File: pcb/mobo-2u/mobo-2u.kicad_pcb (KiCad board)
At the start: 2 copper layers, 71.6 x 83 mm, 69 parts, among them J1 SWD_10, J2 PEEL_MOTOR, J3 DRIVE_MOTOR, J4 SW1, J5 SPRING_FINGERS, J6 SW2, J7 SW1, J8 USART1, J9 SWD_10, U1 STM32F031C6Tx, U2 STM32F031K6Ux, U4 AP1117-33, U5 MC34063AD, U6 MAX3078E, U7 DRV8837, U8 DRV8837, Y1 8MHz

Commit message: mega push, lots of cad updates, new pcb form factor and schematic rework
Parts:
- removed C12: 100uF, Capacitor_SMD:C_Elec_6.3x7.7
- removed C13, C9: 10u, Capacitor_SMD:C_0805_2012Metric
- removed C14: 470pF, Capacitor_SMD:C_0805_2012Metric
- removed D1: LED_RGBA, index:MHS110FRGBCT
- removed D6: 1N5819, Diode_SMD:D_SOD-123
- removed the G*** at (109.3, 62.5)
- removed the G*** at (80.0, 72.5)
- removed J4, J7: SW1, feeder:1TS003B-1400-3500A-CT
- removed J6: SW2, feeder:1TS003B-1400-3500A-CT
- removed L1: 220uH, Inductor_SMD:L_6.3x6.3_H3
- removed R2, R3, R5: 470, Resistor_SMD:R_0805_2012Metric
- removed REF**: OSHW-Symbol_6.7x6mm_Mask, feeder:OSHW-Symbol_6.7x6mm_Mask
- removed U1: STM32F031C6Tx, Package_QFP:LQFP-48_7x7mm_P0.5mm
- removed U4: AP1117-33, Package_TO_SOT_SMD:SOT-223-3_TabPin2
- added C15: 10u, Capacitor_SMD:C_0805_2012Metric, F.Cu at (89.3, 129.3)
- added C21: 10u, Capacitor_SMD:C_0805_2012Metric, F.Cu at (86.8, 129.3)
- added C22: 4.7n, Capacitor_SMD:C_0805_2012Metric, F.Cu at (81.3, 118.8)
- added C23: 47p, Capacitor_SMD:C_0805_2012Metric, F.Cu at (80.0, 115.8)
- added C24: 100n, Capacitor_SMD:C_0805_2012Metric, F.Cu at (83.5, 130.1)
- added C25: 10u, Capacitor_SMD:C_0805_2012Metric, F.Cu at (69.8, 117.3)
- added C26: 10u, Capacitor_SMD:C_0805_2012Metric, F.Cu at (69.8, 119.5)
- added C27: 10u, Capacitor_SMD:C_0805_2012Metric, F.Cu at (69.8, 115.0)
- added C28: 10u, Capacitor_SMD:C_0805_2012Metric, F.Cu at (75.6, 111.0)
- added C29: 0.1n, Capacitor_SMD:C_0805_2012Metric, F.Cu at (80.0, 113.3)
- added D4: B560C, Diode_SMD:D_SMC, F.Cu at (67.4, 126.5)
- added L2: 8.2uH, Inductor_SMD:L_Taiyo-Yuden_NR-50xx, F.Cu at (74.0, 124.7)
- added R10: 4.7k, Resistor_SMD:R_0805_2012Metric, F.Cu at (86.8, 124.0)
- added R11: 243k, Resistor_SMD:R_0805_2012Metric, F.Cu at (83.5, 122.0)
- added R12: 16.9k, Resistor_SMD:R_0805_2012Metric, F.Cu at (78.8, 118.8)
- added R18: 10k, Resistor_SMD:R_0805_2012Metric, F.Cu at (75.6, 120.5)
- added R19: 820R, Resistor_SMD:R_0805_2012Metric, F.Cu at (79.5, 122.0)
- added R8: 10k, Resistor_SMD:R_0805_2012Metric, F.Cu at (89.3, 124.0)
- added SW3: BACK_BTN, feeder:SKTDLDE010, F.Cu at (50.9, 99.3)
- added SW4: FWD_BTN, feeder:SKTDLDE010, F.Cu at (50.9, 83.0)
- added SW5: RESET_BTN, feeder:SKTDLDE010, F.Cu at (116.0, 55.8)
- added U3: STM32F030C8Tx, Package_QFP:LQFP-48_7x7mm_P0.5mm, F.Cu at (96.2, 107.9)
- added U9: TPS54560BDDA, Package_SO:Texas_R-PDSO-G8_EP2.95x4.9mm_Mask2.4x3.1mm_ThermalVias, F.Cu at (81.5, 126.0)
- added VDC: TP_24V, TestPoint:TestPoint_Pad_D2.0mm, F.Cu at (89.3, 120.4)
- C16: value 470uF -> 1u; footprint Capacitor_SMD:C_Elec_6.3x7.7 -> Capacitor_SMD:C_0805_2012Metric
- J9: footprint feeder:SWD-No-Paste -> Connector_PinHeader_1.27mm:PinHeader_2x05_P1.27mm_Vertical_SMD
- R13: value 0.33R -> 470
- R6: value 5.6k -> 470
- R9: value 39k -> 470
- U2: value STM32F031K6Ux -> MHS110FRGBCT; footprint feeder:QFN-32-No-Paste -> index:MHS110FRGBCT
- U5: value MC34063AD -> AP2210; footprint Package_SO:SOIC-8_3.9x4.9mm_P1.27mm -> Package_TO_SOT_SMD:SOT-23-5
- moved U2 53.9 mm to (95.4, 54.6), turned to 180 degrees
- moved PM1 27.9 mm to (61.8, 67.5)
- moved J2 26.4 mm to (60.0, 73.8), turned to -45 degrees
- moved PM2 23.9 mm to (65.0, 71.0)
- moved R6 23.3 mm to (82.8, 106.7), turned to 180 degrees
- moved R9 23.2 mm to (82.8, 104.5), turned to 180 degrees
- moved R13 18.9 mm to (82.8, 102.3), turned to 180 degrees
- moved R17 13.2 mm to (109.6, 57.1)
- moved U5 11.4 mm to (75.5, 114.5), turned to 90 degrees
- moved C16 9.61 mm to (75.5, 118.0)
- moved R7 7.86 mm to (100.4, 93.4), turned to 180 degrees
- moved 10v 7.50 mm to (62.2, 122.3)
- moved J9 3.68 mm to (107.0, 113.7)
- moved C20 3.66 mm to (101.5, 87.5), turned to 135 degrees
- moved C17 3.50 mm to (105.4, 88.8)
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- renumbered TP2 to 10v, TP1 to 3v3, TP3 to DM1, TP4 to DM2, TP6 to PM1, TP5 to PM2, TP8 to QUAD_A, TP7 to QUAD_B
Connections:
- J3 pad MP: (no net) -> GND
- R13 pad 1: +VDC -> LED_B
- R13 pad 2: Net-(U5-DC) -> Net-(U2-BLUE)
- R6 pad 1: Net-(U5-Vfb) -> LED_R
- R6 pad 2: GND -> Net-(U2-RED)
- R9 pad 1: Net-(U5-Vfb) -> LED_G
- R9 pad 2: +10V -> Net-(U2-GREEN)
- U2 pad 2: OSC_IN -> Net-(U2-BLUE)
- U2 pad 3: OSC_OUT -> Net-(U2-GREEN)
- U2 pad 4: RESET -> Net-(U2-RED)
- U5 pad 1: Net-(U5-DC) -> +10V
- U5 pad 2: Net-(D6-K) -> GND
- U5 pad 3: Net-(U5-TC) -> +10V
- U5 pad 4: GND -> Net-(U5-BYP/ADJ)
- U5 pad 5: Net-(U5-Vfb) -> +3V3
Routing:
- net Net-(U2-RED): track 0.00 -> 64.8 mm, vias 0 -> 2
- net Net-(U2-GREEN): track 0.00 -> 61.3 mm, vias 0 -> 2
- net Net-(U2-BLUE): track 0.00 -> 58.1 mm, vias 0 -> 2
- net +3V3: track 251.3 -> 206.4 mm
- net Net-(D1-GK): track 38.9 -> 0.00 mm, vias 2 -> 0
- net Net-(D1-A): track 38.8 -> 0.00 mm, vias 2 -> 0
- net Net-(D1-BK): track 38.7 -> 0.00 mm, vias 2 -> 0
- net Net-(U5-Vfb): track 27.1 -> 0.00 mm, vias 2 -> 0
- net Net-(D4-K): track 0.00 -> 21.5 mm, vias 0 -> 2
- net SW1: track 62.4 -> 43.1 mm
- net SW2: track 66.7 -> 49.7 mm, vias 3 -> 2
- net MOTOR_ENABLE: track 50.9 -> 35.7 mm
- net Net-(D6-K): track 14.9 -> 0.00 mm
- net Net-(U9-COMP): track 0.00 -> 12.4 mm, vias 0 -> 2
- net Net-(U5-DC): track 9.50 -> 0.00 mm
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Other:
- board size 71.6 x 83 mm -> 71.6 x 84.8 mm

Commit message: small tweaks
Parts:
- removed 3v3: TP_3V3, TestPoint:TestPoint_Pad_D2.0mm
- removed C16: 1u, Capacitor_SMD:C_0805_2012Metric
- removed C28: 10u, Capacitor_SMD:C_0805_2012Metric
- removed C29: 0.1n, Capacitor_SMD:C_0805_2012Metric
- removed U5: AP2210, Package_TO_SOT_SMD:SOT-23-5
- added C30: 10uF, Capacitor_SMD:C_0805_2012Metric, F.Cu at (76.7, 115.7)
- added C31: 100nF, Capacitor_SMD:C_0805_2012Metric, F.Cu at (79.1, 109.5)
- added C32: 22uF, Capacitor_SMD:C_0805_2012Metric, F.Cu at (84.8, 114.0)
- added C33: 22uF, Capacitor_SMD:C_0805_2012Metric, F.Cu at (81.3, 115.7)
- added L1: 3.9uH, Inductor_SMD:L_Changjiang_FNR3015S, F.Cu at (81.3, 112.5)
- added TP10: TP_3V3, TestPoint:TestPoint_Pad_D2.0mm, F.Cu at (88.7, 155.4)
- added U1: AP63203WU, Package_TO_SOT_SMD:TSOT-23-6, F.Cu at (76.7, 112.5)
- moved C23 7.52 mm to (86.6, 119.5), turned to 180 degrees
- moved C22 1.75 mm to (82.9, 119.5), turned to 0 degrees
- moved TP9 1.30 mm to (90.6, 120.5)
- moved R12 0.81 mm to (79.2, 119.5), turned to 0 degrees
- renumbered 10v to TP2, DM1 to TP3, DM2 to TP4, PM2 to TP5, PM1 to TP6, QUAD_B to TP7, QUAD_A to TP8, VDC to TP9
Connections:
- J3 pad MP: GND -> (no net)
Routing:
- net Net-(U9-COMP): track 12.4 -> 18.9 mm
- net Net-(U1-SW): track 0.00 -> 5.20 mm
- net Net-(U5-BYP/ADJ): track 2.65 -> 0.00 mm
- net +3V3: track 206.4 -> 208.5 mm, vias 8 -> 10
- net Net-(U1-BST): track 0.00 -> 1.90 mm
- net +10V: track 97.1 -> 98.1 mm
- net Net-(C22-Pad1): track 2.52 -> 1.84 mm
- net +VDC: track 37.9 -> 37.3 mm
- net GND: track 42.3 -> 42.1 mm, vias 112 -> 98

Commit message: rev00b1 pcb, working cad. about to try to test parametric for 16mm
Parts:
- removed J9: SWD_10, Connector_PinHeader_1.27mm:PinHeader_2x05_P1.27mm_Vertical_SMD
- added D1: SMF28A, Diode_SMD:D_SMF, F.Cu at (92.4, 125.2)
- added D3: PESD3V3S1UL, Diode_SMD:D_SOD-882, F.Cu at (100.8, 128.9)
- added D5: PESD3V3S1UL, Diode_SMD:D_SOD-882, F.Cu at (103.3, 128.9)
- added D6: PESD3V3S1UL, Diode_SMD:D_SOD-882, F.Cu at (98.3, 128.9)
- added G***: LOGO, index:goblin, F.Cu at (84.5, 70.3)
- added TP1: TP_RESET, TestPoint:TestPoint_Pad_D2.0mm, F.Cu at (103.7, 112.7)
- added TP11: TP_SWCLK, TestPoint:TestPoint_Pad_D2.0mm, F.Cu at (82.2, 103.9)
- added TP12: TP_SWDIO, TestPoint:TestPoint_Pad_D2.0mm, F.Cu at (84.0, 101.2)
- added U4: ~, Package_TO_SOT_SMD:SOT-23, F.Cu at (83.3, 56.4)
- J2: footprint Connector_Molex:Molex_PicoBlade_53261-0271_1x02-1MP_P1.25mm_Horizontal -> Connector_Molex:Molex_PicoBlade_53398-0271_1x02-1MP_P1.25mm_Vertical
- moved SW5 92.4 mm to (63.3, 131.7), turned to 180 degrees
- moved R17 83.8 mm to (68.8, 130.3), turned to 180 degrees
- moved SW4 71.8 mm to (116.7, 54.4), turned to 0 degrees
- moved SW3 59.7 mm to (90.2, 54.4), turned to 0 degrees
- moved R6 51.1 mm to (101.3, 59.1), turned to 90 degrees
- moved R9 49.9 mm to (103.5, 59.1), turned to 90 degrees
- moved R13 49.8 mm to (106.4, 58.4)
- moved TP10 48.6 mm to (82.0, 107.3)
- moved J1 31.7 mm to (75.5, 101.9), turned to 135 degrees
- moved TP6 28.6 mm to (61.7, 96.1), turned to 90 degrees
- moved J2 26.5 mm to (54.7, 99.7), turned to 45 degrees
- moved TP5 24.4 mm to (54.1, 92.9), turned to 90 degrees
- moved C1 19.0 mm to (89.6, 114.4), turned to -45 degrees
- moved C3 17.5 mm to (85.5, 105.7), turned to 0 degrees
- moved C11 16.6 mm to (85.5, 107.9), turned to 0 degrees
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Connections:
- U3 pad 10: PA0 -> ~{RE}
- U3 pad 11: PA1 -> DE
- U3 pad 12: MOTOR_ENABLE -> PHOTON_TX
- U3 pad 13: PA3 -> PHOTON_RX
- U3 pad 14: LED_B -> DRIVE_QUAD_A
- U3 pad 15: unconnected-(U3-PA5-Pad15) -> DRIVE_QUAD_B
- U3 pad 16: LED_G -> DRIVE1
- U3 pad 17: LED_R -> DRIVE2
- U3 pad 18: SW2 -> LED_R
- U3 pad 19: SW1 -> LED_G
- U3 pad 20: unconnected-(U3-PB2-Pad20) -> FILM_TENSION
- U3 pad 3: unconnected-(U3-PC14-Pad3) -> OSC_IN
- U3 pad 32: ~{RE} -> unconnected-(U3-PA11-Pad32)
- U3 pad 33: DE -> unconnected-(U3-PA12-Pad33)
- U3 pad 38: PEEL2 -> unconnected-(U3-PA15-Pad38)
- U3 pad 39: PEEL1 -> unconnected-(U3-PB3-Pad39)
- U3 pad 4: unconnected-(U3-PC15-Pad4) -> OSC_OUT
- U3 pad 40: DRIVE1 -> LED_B
- U3 pad 41: DRIVE2 -> SW2
- U3 pad 42: DRIVE_QUAD_A -> SW1
- U3 pad 43: DRIVE_QUAD_B -> MOTOR_ENABLE
- U3 pad 45: unconnected-(U3-PB8-Pad45) -> PEEL1
- U3 pad 46: unconnected-(U3-PB9-Pad46) -> PEEL2
- U3 pad 5: OSC_IN -> unconnected-(U3-PF0-Pad5)
- U3 pad 6: OSC_OUT -> unconnected-(U3-PF1-Pad6)
- U6 pad 1: MCU_RX -> PHOTON_RX
- U6 pad 4: MCU_TX -> PHOTON_TX
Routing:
- net FILM_TENSION: track 0.00 -> 65.0 mm, vias 0 -> 2
- net Net-(U2-RED): track 64.8 -> 2.32 mm, vias 2 -> 0
- net Net-(U2-GREEN): track 61.3 -> 1.88 mm, vias 2 -> 0
- net Net-(U2-BLUE): track 58.1 -> 2.58 mm, vias 2 -> 0
- net LED_R: track 8.53 -> 58.6 mm
- net LED_G: track 9.24 -> 58.1 mm
- net LED_B: track 9.75 -> 56.5 mm
- net +3V3: track 208.5 -> 243.7 mm
- net MCU_TX: track 23.2 -> 48.3 mm
- net RESET: track 22.7 -> 43.2 mm, vias 4 -> 1
- net BOOT0: track 66.8 -> 47.2 mm
- net PEEL2: track 30.5 -> 14.8 mm
- net PHOTON_RX: track 0.00 -> 15.6 mm, vias 0 -> 2
- net MCU_RX: track 32.5 -> 48.1 mm
- net SW1: track 43.1 -> 57.6 mm
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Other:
- board size 71.6 x 84.8 mm -> 71.6 x 80 mm
- board text added: "LumenPnP 2u Feeder REV00b1 Opulo Inc."
- board text removed: "LumenPnP 2u Feeder REV00b0 Opulo Inc."

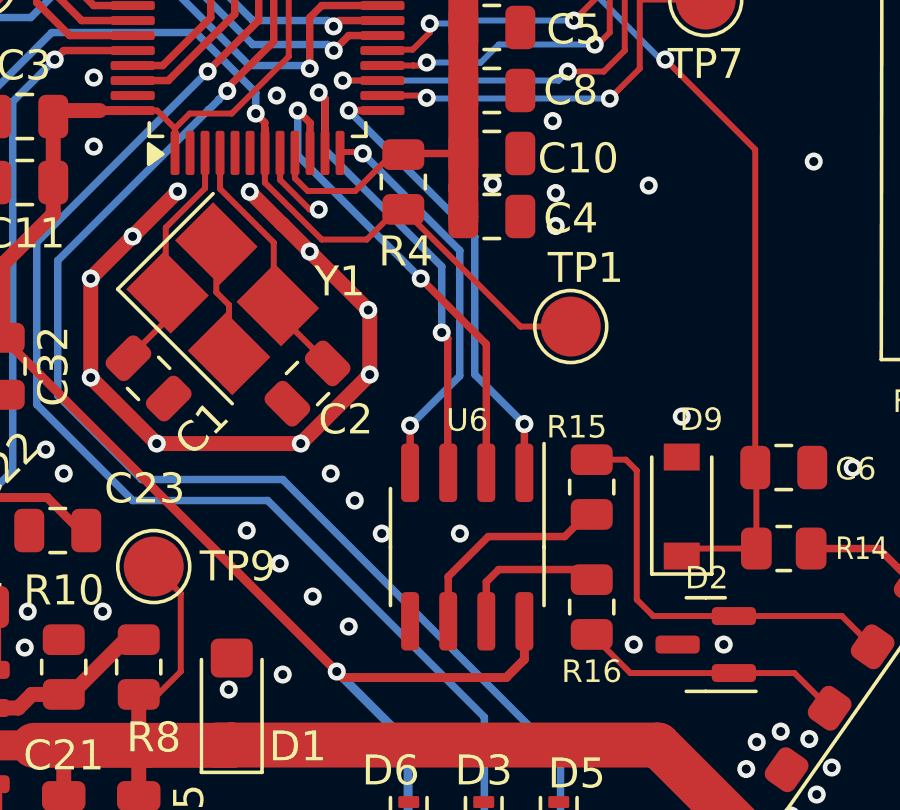
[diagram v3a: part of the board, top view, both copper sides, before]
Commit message: few more geometry tweaks, makes peel gear disengage fully
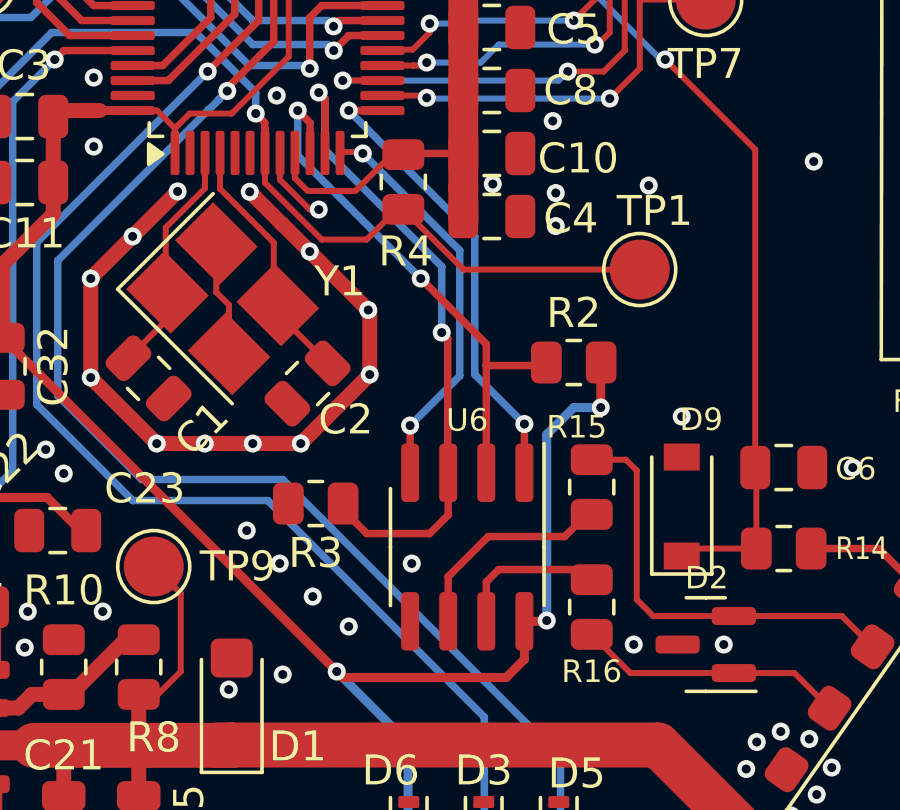
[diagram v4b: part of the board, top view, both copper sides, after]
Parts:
- added R2: 1M, Resistor_SMD:R_0805_2012Metric, F.Cu at (103.8, 113.9)
- added R3: 1M, Resistor_SMD:R_0805_2012Metric, F.Cu at (95.2, 118.6)
- moved TP1 2.98 mm to (106.0, 110.8)
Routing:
- net +3V3: track 243.7 -> 254.4 mm, vias 10 -> 12
- net DE: track 16.6 -> 22.3 mm
- net ~{RE}: track 16.3 -> 18.3 mm
- net RESET: track 43.2 -> 44.7 mm
- net GND: vias 111 -> 110

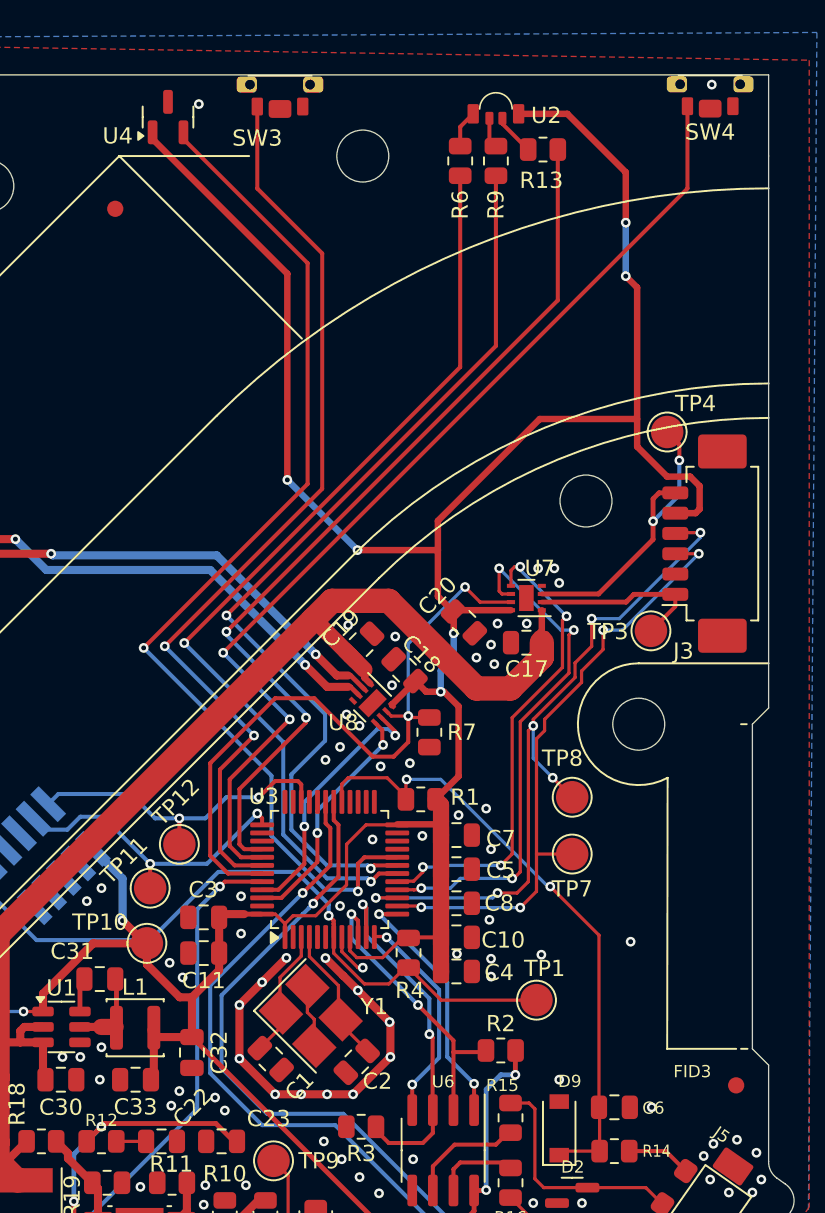
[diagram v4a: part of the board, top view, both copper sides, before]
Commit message: tweaks to pcb, adds supportless features to frame, id fid slot
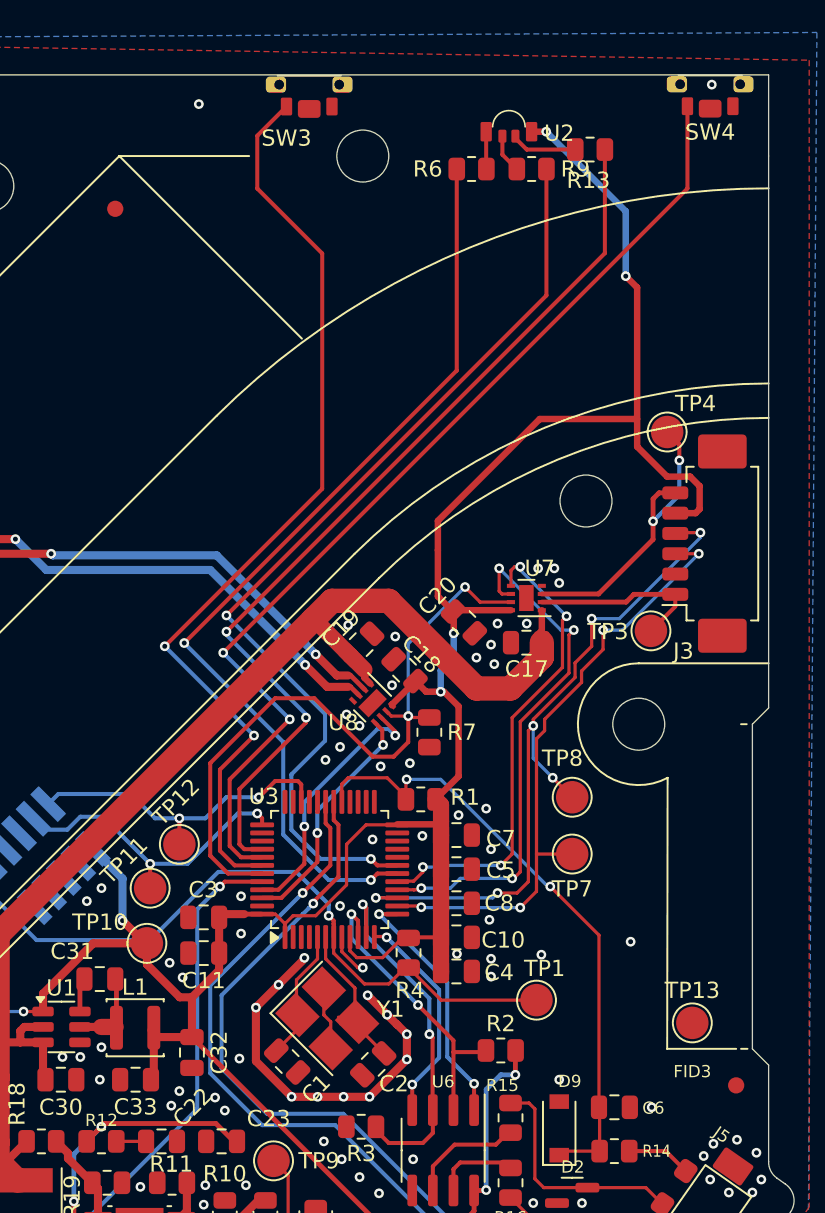
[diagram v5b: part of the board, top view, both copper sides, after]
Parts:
- removed the G*** at (84.5, 70.3)
- removed U4: ~, Package_TO_SOT_SMD:SOT-23
- added TP13: TP_RESET, TestPoint:TestPoint_Pad_D2.0mm, F.Cu at (115.6, 112.2)
- moved R13 2.90 mm to (109.3, 58.4)
- moved R9 2.26 mm to (105.7, 59.6), turned to 180 degrees
- moved SW3 1.80 mm to (92.0, 54.4)
- moved U2 1.36 mm to (104.3, 56.9)
- moved C1 1.03 mm to (90.6, 114.6)
- moved Y1 1.03 mm to (93.1, 111.9)
- moved C2 1.03 mm to (95.9, 114.8)
- moved R6 0.86 mm to (102.0, 59.6), turned to 0 degrees
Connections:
- U3 pad 3: OSC_IN -> unconnected-(U3-PC14-Pad3)
- U3 pad 4: OSC_OUT -> unconnected-(U3-PC15-Pad4)
- U3 pad 5: unconnected-(U3-PF0-Pad5) -> OSC_IN
- U3 pad 6: unconnected-(U3-PF1-Pad6) -> OSC_OUT
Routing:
- net FILM_TENSION: track 65.0 -> 0.00 mm, vias 2 -> 0
- net +3V3: track 254.4 -> 215.8 mm, vias 12 -> 10
- net GND: track 38.7 -> 35.9 mm
- net LED_G: track 58.1 -> 59.7 mm
- net Net-(U2-BLUE): track 2.58 -> 4.10 mm
- net LED_B: track 56.5 -> 57.7 mm
- net SW1: track 57.6 -> 58.4 mm
- net Net-(U2-GREEN): track 1.88 -> 2.39 mm

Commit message: this commit reflects rev00b2 pcb
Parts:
- removed C15, C21, C25, C26, C27: 10u, Capacitor_SMD:C_0805_2012Metric
- removed C22: 4.7n, Capacitor_SMD:C_0805_2012Metric
- removed C23: 47p, Capacitor_SMD:C_0805_2012Metric
- removed C24: 100n, Capacitor_SMD:C_0805_2012Metric
- removed D1: SMF28A, Diode_SMD:D_SMF
- removed D4: B560C, Diode_SMD:D_SMC
- removed L2: 8.2uH, Inductor_SMD:L_Taiyo-Yuden_NR-50xx
- removed R10: 4.7k, Resistor_SMD:R_0805_2012Metric
- removed R11: 243k, Resistor_SMD:R_0805_2012Metric
- removed R12: 16.9k, Resistor_SMD:R_0805_2012Metric
- removed R18, R8: 10k, Resistor_SMD:R_0805_2012Metric
- removed R19: 820R, Resistor_SMD:R_0805_2012Metric
- removed TP2: TP_10V, TestPoint:TestPoint_Pad_D2.0mm
- removed U9: TPS54560BDDA, Package_SO:Texas_R-PDSO-G8_EP2.95x4.9mm_Mask2.4x3.1mm_ThermalVias
- added C12: 100nF, Capacitor_SMD:C_0805_2012Metric, F.Cu at (76.7, 126.9)
- added C13: 56pF, Capacitor_SMD:C_0805_2012Metric, F.Cu at (87.0, 126.1)
- added C14: 22uF, Capacitor_SMD:C_0805_2012Metric, F.Cu at (76.5, 118.2)
- added C16: 22uF, Capacitor_SMD:C_0805_2012Metric, F.Cu at (76.5, 120.6)
- added C9: 10uF, Capacitor_SMD:C_0805_2012Metric, F.Cu at (81.0, 120.6)
- added D7: SMF28A, Diode_SMD:D_SMF, F.Cu at (84.6, 120.7)
- added G***: LOGO, index:goblin, F.Cu at (70.0, 128.5)
- added L3: 10uH, Inductor_SMD:L_Changjiang_FNR3015S, F.Cu at (76.7, 123.7)
- added R20: 18k, Resistor_SMD:R_0805_2012Metric, F.Cu at (81.0, 126.9)
- added R5: 218k, Resistor_SMD:R_0805_2012Metric, F.Cu at (84.5, 126.1)
- added TP14: TP_10V, TestPoint:TestPoint_Pad_D2.0mm, F.Cu at (72.9, 118.7)
- added U4: AP63200WU, Package_TO_SOT_SMD:TSOT-23-6, F.Cu at (81.0, 123.7)
- moved TP13 46.0 mm to (69.8, 116.3)
- moved R17 6.38 mm to (63.4, 126.9)
- moved TP9 4.74 mm to (93.1, 124.1)
- moved C30 0.22 mm to (76.5, 115.8)
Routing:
- net Net-(D4-K): track 19.7 -> 0.00 mm, vias 2 -> 0
- net Net-(U9-COMP): track 18.9 -> 0.00 mm, vias 2 -> 0
- net +10V: track 92.4 -> 100.3 mm, vias 0 -> 2
- net Net-(U4-FB): track 0.00 -> 7.55 mm
- net Net-(U9-EN): track 6.13 -> 0.00 mm
- net Net-(U4-SW): track 0.00 -> 6.08 mm
- net GND: track 35.9 -> 30.0 mm, vias 110 -> 100
- net Net-(U9-FB): track 5.71 -> 0.00 mm
- net Net-(U4-BST): track 0.00 -> 3.35 mm
- net Net-(U9-BOOT): track 2.26 -> 0.00 mm
- net Net-(U9-RT/CLK): track 2.24 -> 0.00 mm
- net BOOT0: track 47.2 -> 45.3 mm
- net Net-(C22-Pad1): track 1.84 -> 0.00 mm
- net +VDC: track 38.9 -> 37.1 mm
- net +3V3: track 215.8 -> 216.6 mm
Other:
- board text added: "LumenPnP 2u Feeder REV00b2 Opulo Inc."
- board text removed: "LumenPnP 2u Feeder REV00b1 Opulo Inc."

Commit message: updates stickers, tweaks
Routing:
- net +VDC: track 37.1 -> 36.4 mm
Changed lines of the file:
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@@
+	)
+	(segment
+		(start 83.999999 122.750001)
+		(end 83.3 122.750001)
+		(width 1)
+		(layer "F.Cu")
+		(net 4)
 	)
 	(segment
@@
 		(end 82.1375 122.750001)
 		(width 0.2)
-		(layer "F.Cu")
-		(net 4)
-	)
-	(segment
-		(start 82.1375 122.750001)
-		(end 83.999999 122.750001)
-		(width 0.5)
 		(layer "F.Cu")
 		(net 4)
@@
 	)
 	(segment
-		(start 83.999999 122.750001)
-		(end 83.3 122.750001)
-		(width 1)
-		(layer "F.Cu")
-		(net 4)
-	)
-	(segment
 		(start 81.949999 122.5625)
 		(end 82.1375 122.750001)
@@
 		(layer "F.Cu")
 		(net 4)
+	)
+	(segment
+		(start 82.1375 122.750001)
+		(end 83.3 122.750001)
+		(width 0.5)
+		(layer "F.Cu")
+		(net 4)
